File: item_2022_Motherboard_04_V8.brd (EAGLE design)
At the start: 160 x 100 mm, 126 parts, among them IC1 MCP602SN, IC2 LD117AS33TR, IC3 MCP1525TO, IC4 MCP6S26, IC5 MCP6004SO, IC6 MCP6004SO, IC7 MCP3204SL, IC8 LM336LP, IC9 MCP6004SO, U1 ESP32-DEVKITC-32D, U2 ADS1256_BOARD, U3 SSD1306_128X64, X1 MSTBA4, X2 MSTBA4

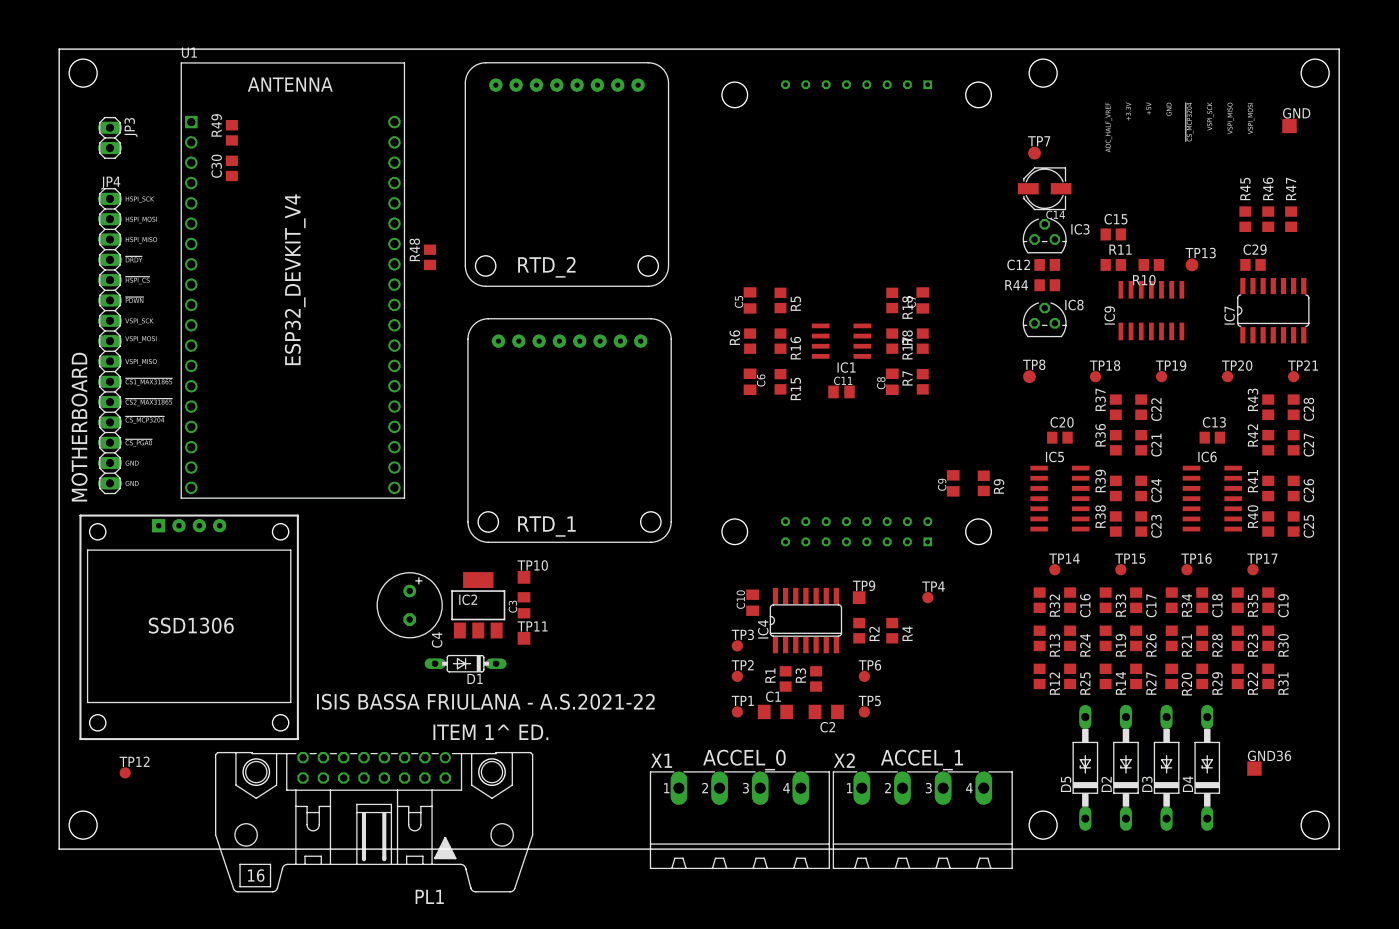
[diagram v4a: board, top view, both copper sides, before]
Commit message: routing with changed PGA inputs
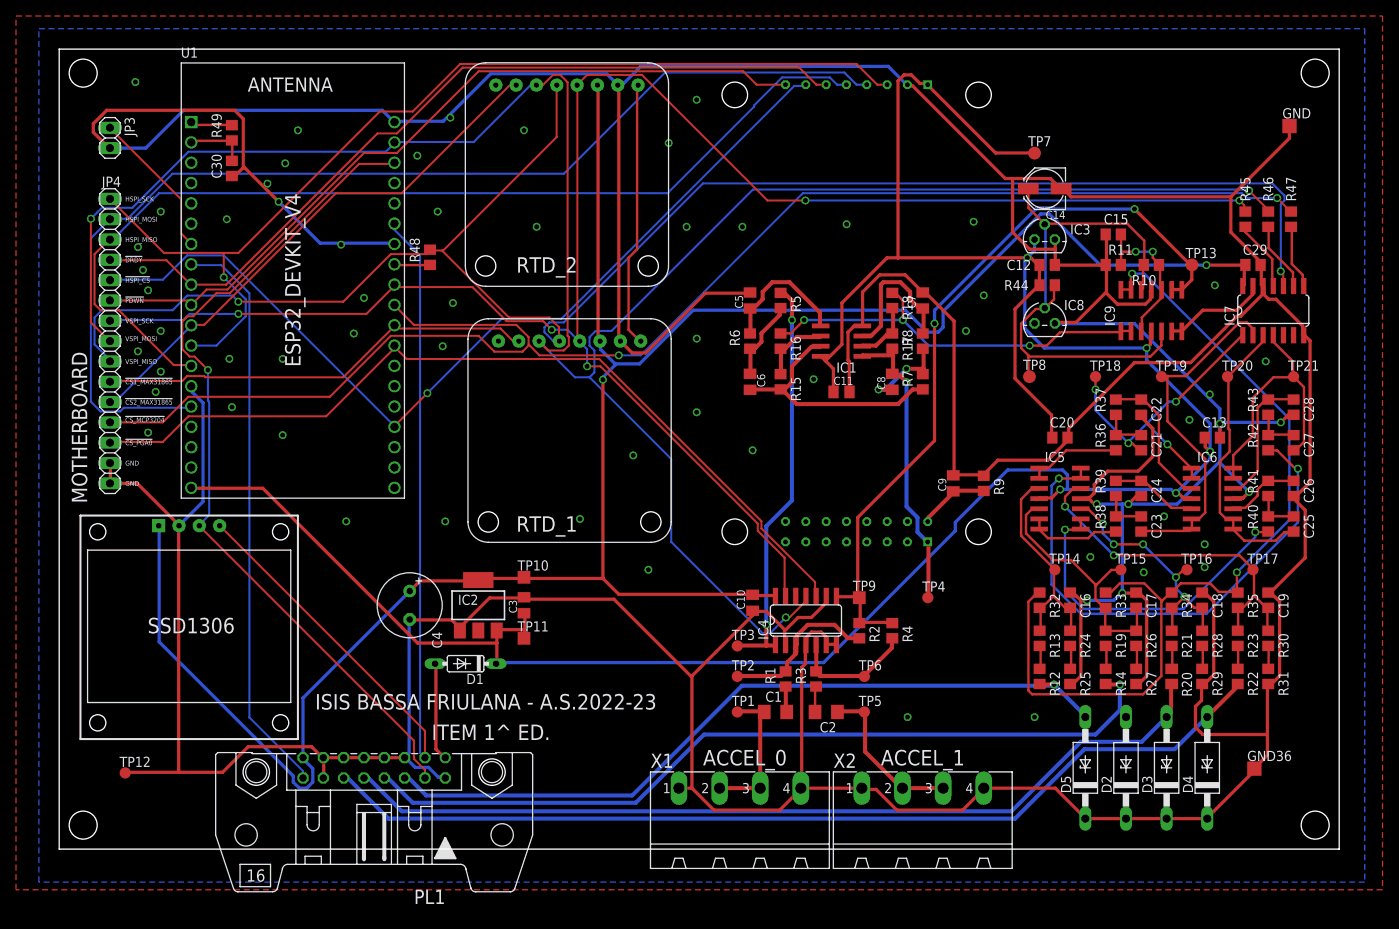
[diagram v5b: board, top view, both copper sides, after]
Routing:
- net GND: track 0.00 -> 974.3 mm, vias 0 -> 62
- net +5V: track 0.00 -> 326.1 mm, vias 0 -> 5
- net +3V3: track 0.00 -> 278.1 mm, vias 0 -> 2
- net VSPI_MOSI: track 0.00 -> 277.5 mm, vias 0 -> 3
- net VSPI_SCK: track 0.00 -> 231.1 mm, vias 0 -> 5
- net VSPI_MISO: track 0.00 -> 216.2 mm, vias 0 -> 2
- net !CS_MCP3204!: track 0.00 -> 182.6 mm, vias 0 -> 2
- net HSPI_MOSI: track 0.00 -> 140.0 mm
- net HSPI_SCK: track 0.00 -> 128.2 mm, vias 0 -> 1
- net HSPI_MISO: track 0.00 -> 125.2 mm
- net SPEED2+: track 0.00 -> 121.0 mm
- net !HSPI_CS!: track 0.00 -> 115.0 mm, vias 0 -> 1
- net +2.5V: track 0.00 -> 114.6 mm, vias 0 -> 2
- net SPEED1+: track 0.00 -> 111.4 mm
- net !CS_PGA0!: track 0.00 -> 108.0 mm
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- added copper zone on layer 1, net GND
- added copper zone on layer 16, net GND
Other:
- board text added: "ISIS BASSA FRIULANA - A.S.2022-23"
- board text removed: "+3.3V"
- board text removed: "+5V"
- board text removed: "ADC_HALF_VREF"
- board text removed: "ISIS BASSA FRIULANA - A.S.2021-22"

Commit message: routing with corrected pads
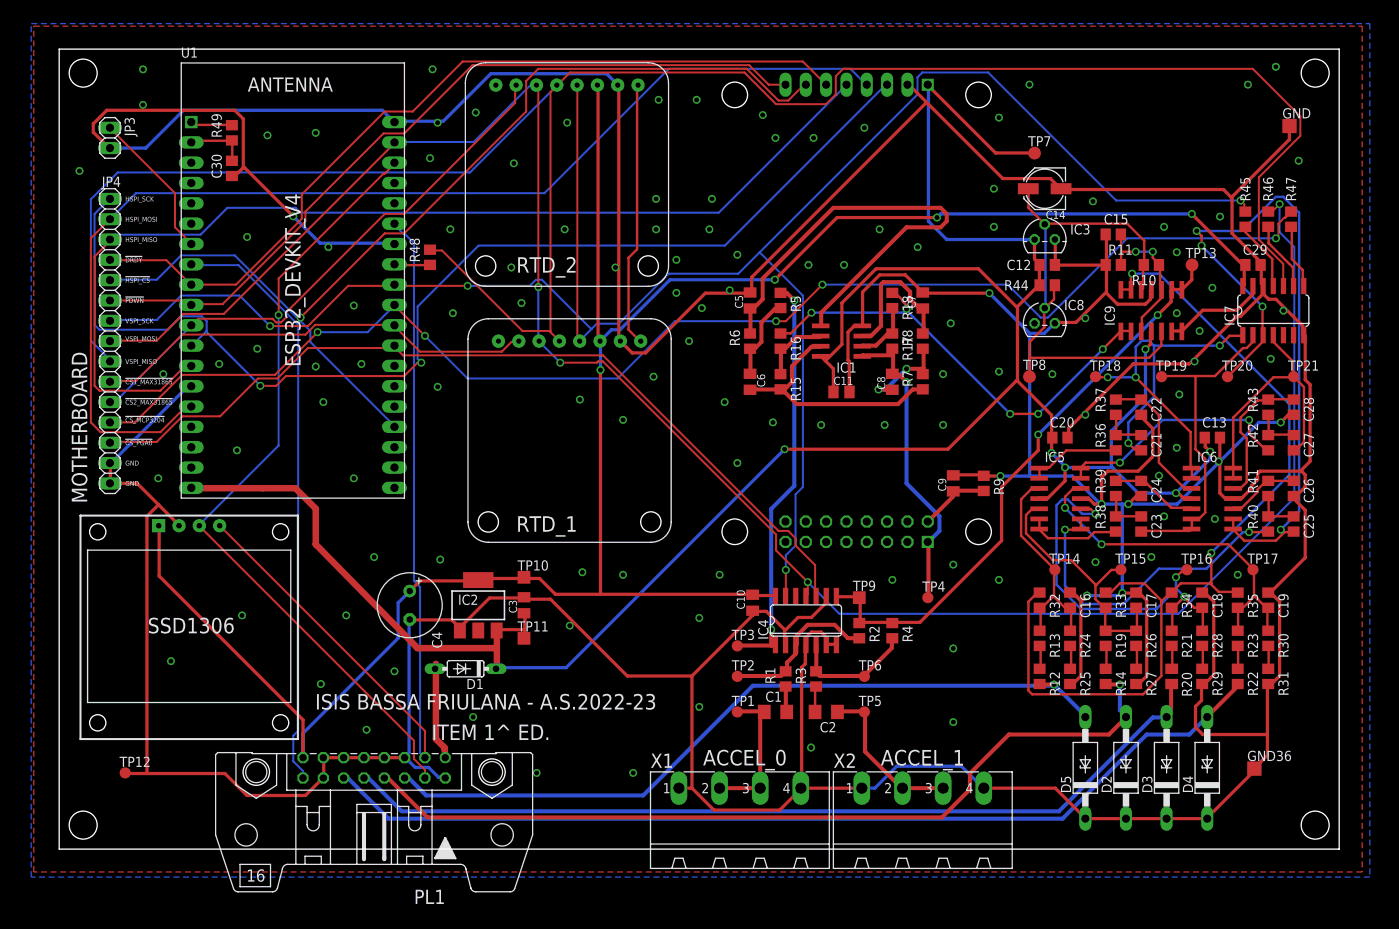
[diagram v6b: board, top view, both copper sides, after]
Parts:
- moved D1 0.63 mm to (50.8, 22.5)
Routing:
- net A_SPEED1: track 36.6 -> 89.9 mm, vias 0 -> 4
- net VSPI_MISO: track 216.2 -> 263.1 mm, vias 2 -> 0
- net N$10: track 17.3 -> 58.0 mm
- net N$31: track 66.0 -> 29.8 mm
- net GND: track 974.3 -> 950.3 mm, vias 62 -> 121
- net ADC_HALF_VREF_A: track 95.8 -> 73.5 mm
- net VSPI_MOSI: track 277.5 -> 255.7 mm, vias 3 -> 4
- net VSPI_SCK: track 231.1 -> 252.6 mm, vias 5 -> 4
- net N$26: track 31.8 -> 50.9 mm, vias 5 -> 3
- net HSPI_SCK: track 128.2 -> 144.1 mm, vias 1 -> 2
- net A_TORQUE1: track 41.2 -> 54.5 mm
- net +5V: track 326.1 -> 312.9 mm, vias 5 -> 6
- net !HSPI_CS!: track 115.0 -> 127.7 mm
- net !CS_MCP3204!: track 182.6 -> 170.6 mm, vias 2 -> 5
- net +3V3: track 278.1 -> 266.8 mm, vias 2 -> 4
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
